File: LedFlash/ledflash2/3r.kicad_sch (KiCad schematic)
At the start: 5 parts

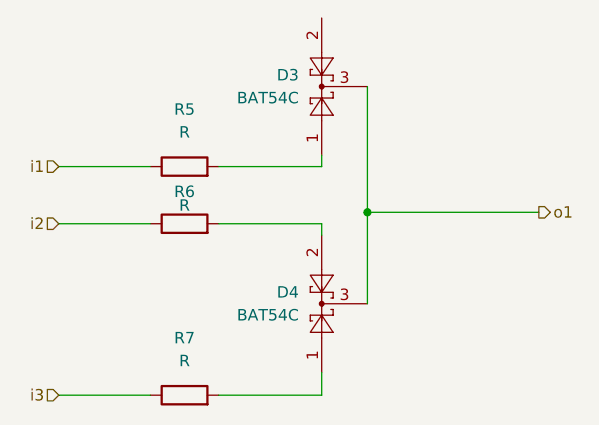
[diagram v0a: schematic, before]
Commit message: Update LED Flash - Added R values, tables and BOM file
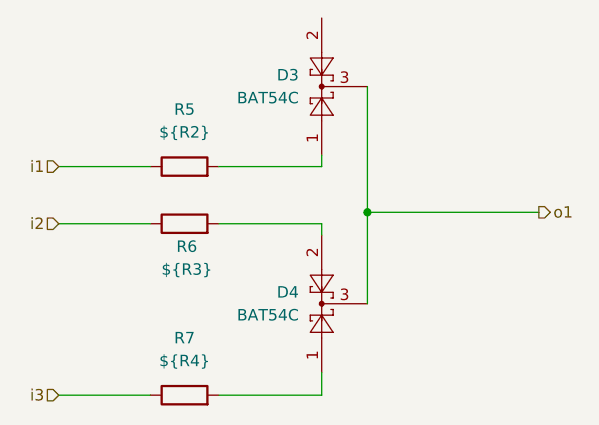
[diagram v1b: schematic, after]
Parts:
- R5: value R -> ${R2}
- R6: value R -> ${R3}
- R7: value R -> ${R4}
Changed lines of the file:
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@@
 			)
 		)
-		(property "Value" "R"
+		(property "Value" "${R4}"
 			(at 111.76 102.87 90)
 			(effects
@@
 		(dnp no)
 		(property "Reference" "R6"
-			(at 111.76 84.074 90)
-			(effects
-				(font
-					(size 1.27 1.27)
-				)
-			)
-		)
-		(property "Value" "R"
-			(at 111.76 85.598 90)
+			(at 112.014 90.17 90)
+			(effects
+				(font
+					(size 1.27 1.27)
+				)
+			)
+		)
+		(property "Value" "${R3}"
+			(at 112.014 92.71 90)
 			(effects
 				(font
@@
 			)
 		)
-		(property "Value" "R"
+		(property "Value" "${R2}"
 			(at 111.76 77.47 90)
 			(effects
